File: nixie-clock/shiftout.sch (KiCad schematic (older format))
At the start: 24 parts

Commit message: Added footprints for mini360 buck and nichicon 1uf 250v film cap. Updated nixie-clock schematic with values. Starting to update schematic with daisy-chained configuration now that I figured out the problem with the circuit.
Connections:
- wire segments 171 -> 177
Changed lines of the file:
@@
 Text Notes 5850 3000 0    50   ~ 0
 IN-1\nHours
+Wire Wire Line
+	950  1950 950  2650
+Wire Wire Line
+	950  2650 1400 2650
+Connection ~ 1400 2650
+Wire Wire Line
+	950  5700 950  6400
+Wire Wire Line
+	950  6400 1400 6400
+Connection ~ 1400 6400
+Wire Wire Line
+	5850 4100 5850 4800
+Wire Wire Line
+	5850 4800 6300 4800
+Connection ~ 6300 4800
 $EndSCHEMATC

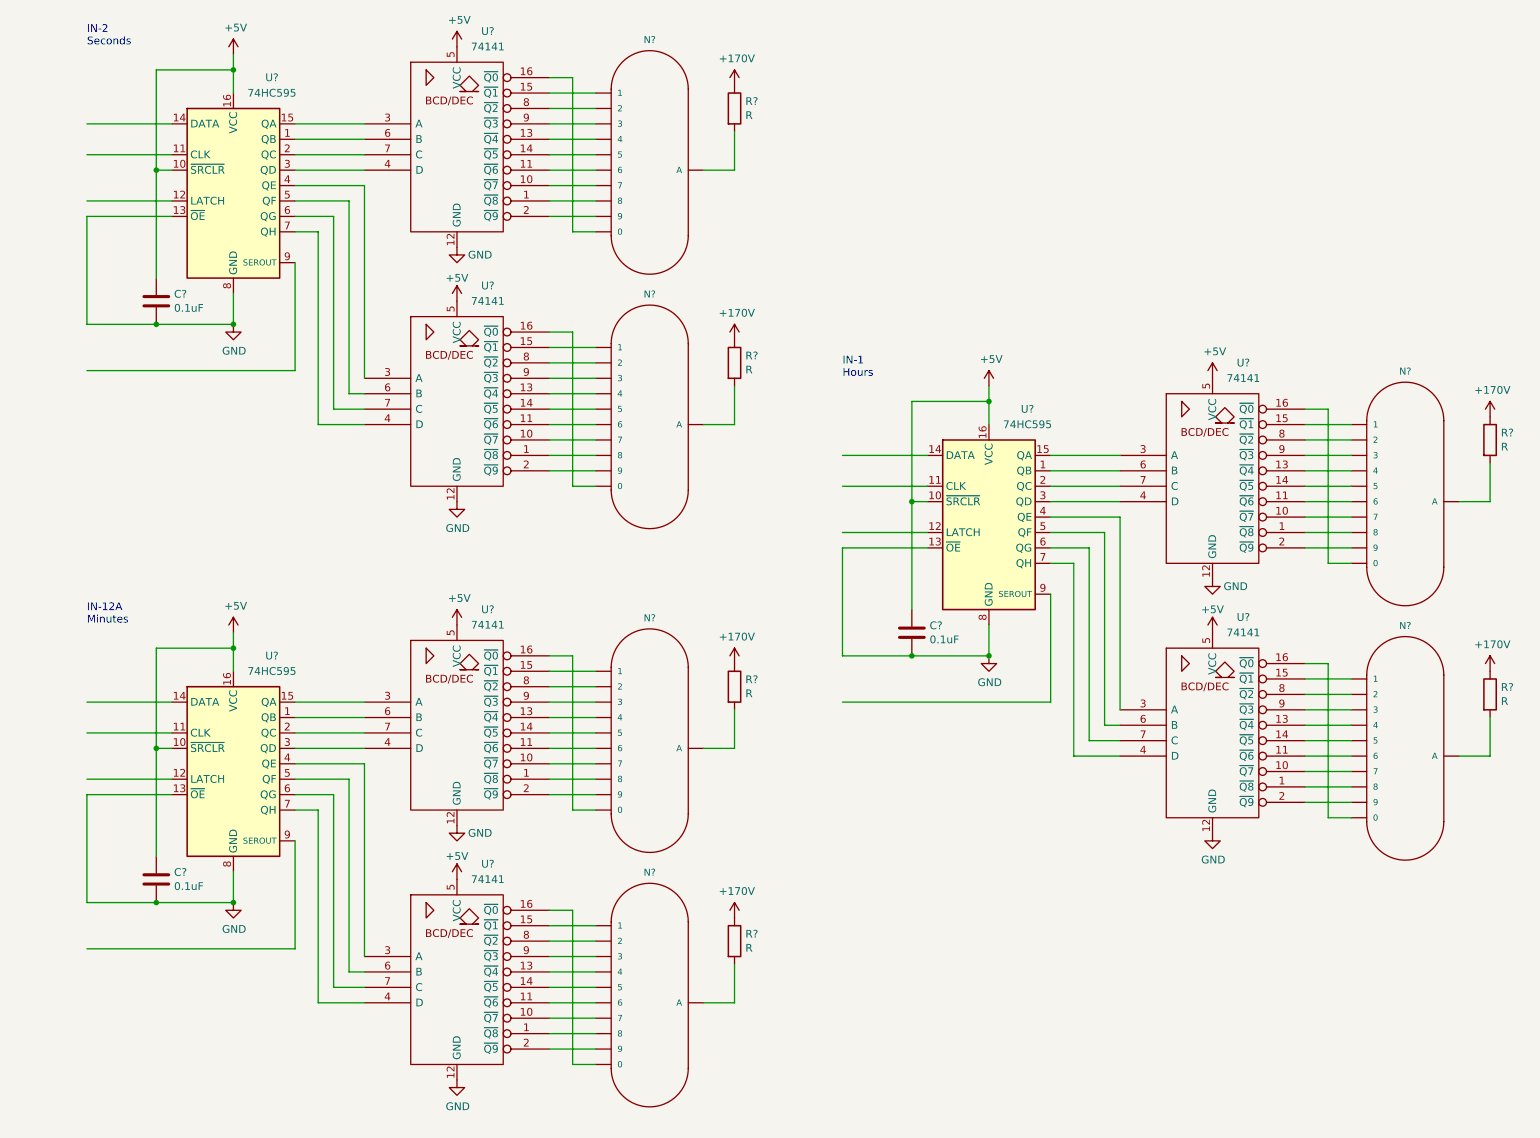
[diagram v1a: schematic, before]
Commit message: Finished schematic for nixie clock main board. Added IN-3 footprint.
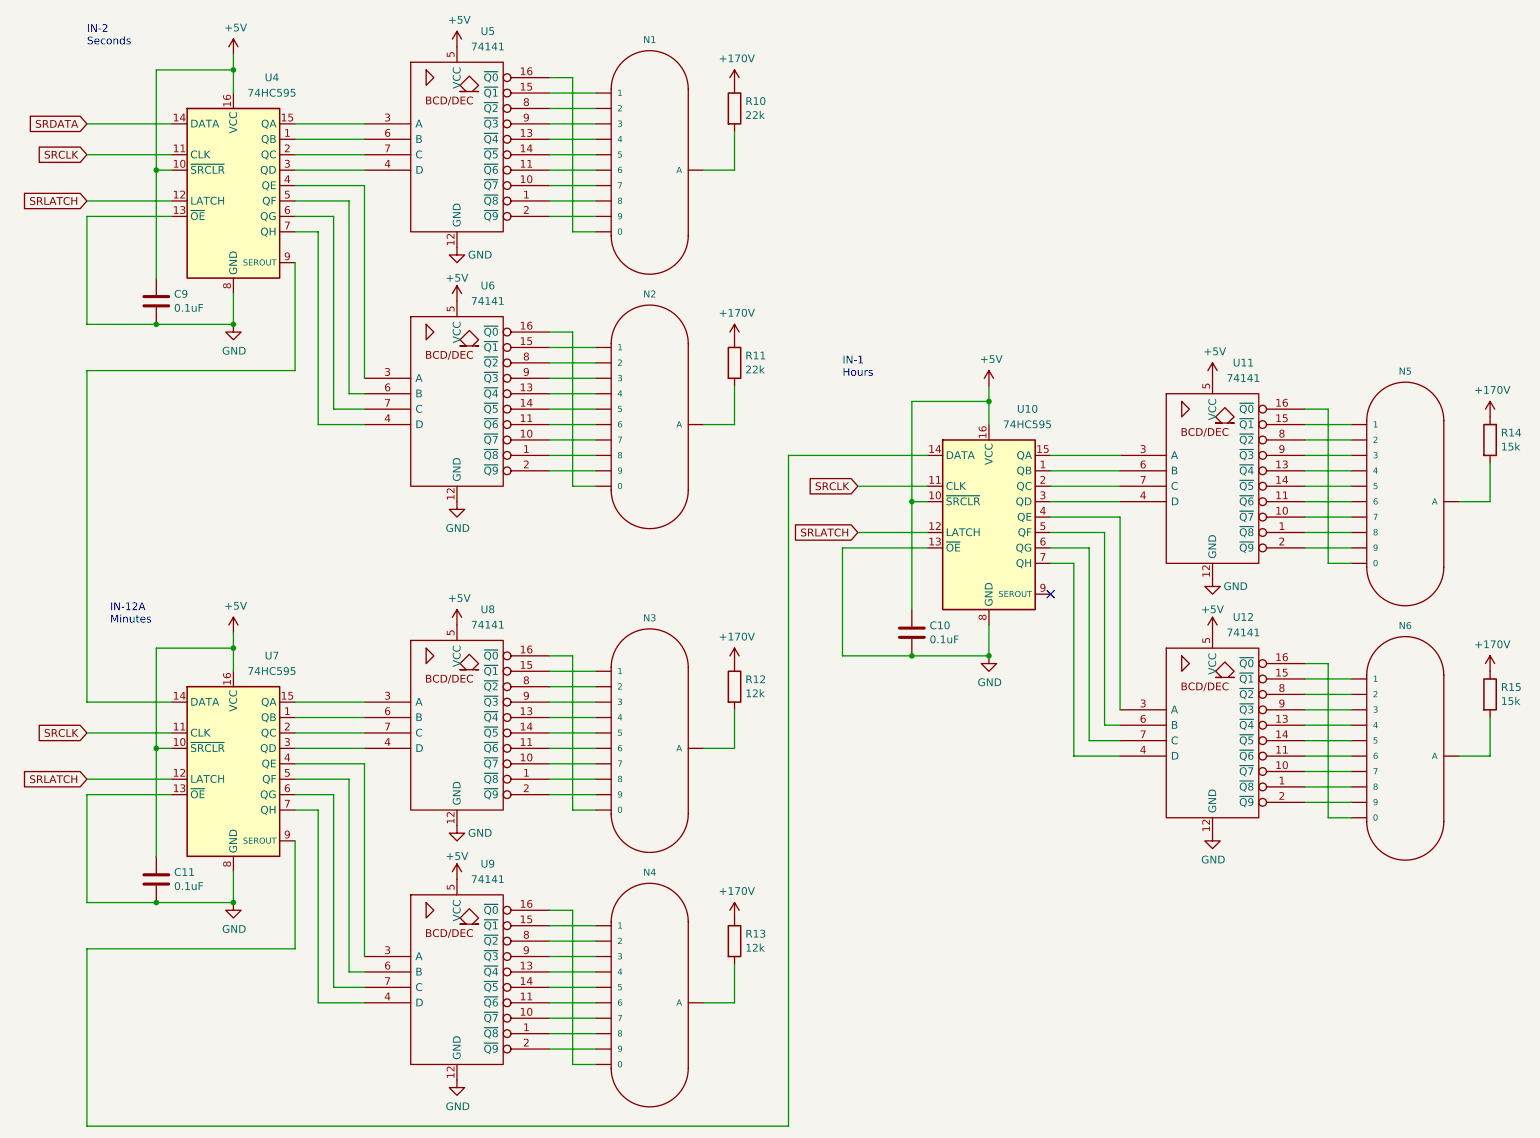
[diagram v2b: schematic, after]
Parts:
- C10, C11, C9: renamed from C?; footprint (none) -> Capacitor_THT:C_Disc_D5.0mm_W2.5mm_P5.00mm
- R10, R11: renamed from R?; value R -> 22k; footprint (none) -> Resistor_THT:R_Axial_DIN0207_L6.3mm_D2.5mm_P10.16mm_Horizontal
- R12, R13: renamed from R?; value R -> 12k; footprint (none) -> Resistor_THT:R_Axial_DIN0207_L6.3mm_D2.5mm_P10.16mm_Horizontal
- R14, R15: renamed from R?; value R -> 15k; footprint (none) -> Resistor_THT:R_Axial_DIN0207_L6.3mm_D2.5mm_P10.16mm_Horizontal
- U10, U11, U12, U4, U5, U6, U7, U8, U9: renamed from U?; footprint (none) -> Package_DIP:DIP-16_W7.62mm_Socket
- gave numbers to parts that had none: 6
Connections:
- net labels added: SRCLK, SRDATA, SRLATCH
- wire segments 177 -> 179
- no-connect marks 0 -> 1

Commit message: Readded pushbuttons to mainboard as an option. Beginning K155ID1-nixie exchange zone.
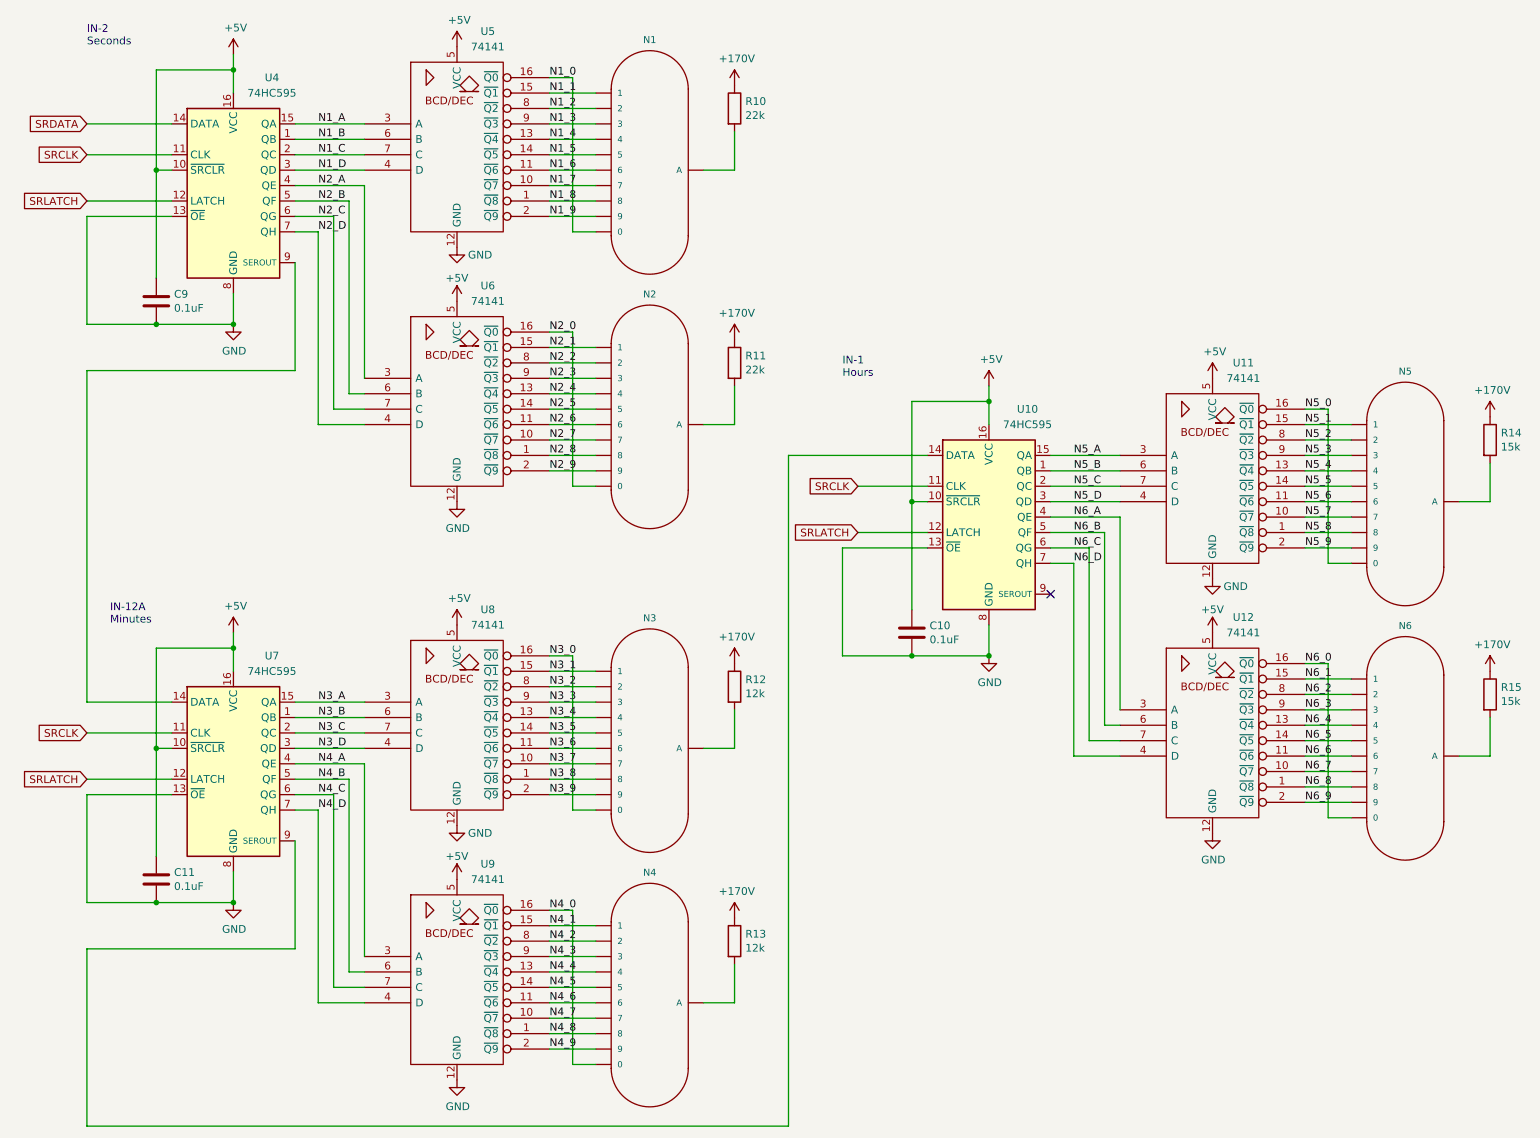
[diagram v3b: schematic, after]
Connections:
- net N2_8: now reaches N2.8, U6.1 (~Q8)
- net N2_7: now reaches N2.7, U6.10 (~Q7)
- net N2_6: now reaches N2.6, U6.11 (~Q6)
- net N2_4: now reaches N2.4, U6.13 (~Q4)
- net N2_5: now reaches N2.5, U6.14 (~Q5)
- net N2_1: now reaches N2.1, U6.15 (~Q1)
- net N2_0: now reaches N2.0, U6.16 (~Q0)
- net N2_9: now reaches N2.9, U6.2 (~Q9)
- net N2_A: now reaches U4.4 (QE), U6.3 (A)
- net N2_D: now reaches U4.7 (QH), U6.4 (D)
- net N2_B: now reaches U4.5 (QF), U6.6 (B)
- net N2_C: now reaches U4.6 (QG), U6.7 (C)
- net N2_2: now reaches N2.2, U6.8 (~Q2)
- net N2_3: now reaches N2.3, U6.9 (~Q3)
- net N1_8: now reaches N1.8, U5.1 (~Q8)
- net N1_7: now reaches N1.7, U5.10 (~Q7)
- net N1_6: now reaches N1.6, U5.11 (~Q6)
- net N1_4: now reaches N1.4, U5.13 (~Q4)
- net N1_5: now reaches N1.5, U5.14 (~Q5)
- net N1_1: now reaches N1.1, U5.15 (~Q1)
- net N1_0: now reaches N1.0, U5.16 (~Q0)
- net N1_9: now reaches N1.9, U5.2 (~Q9)
- net N1_A: now reaches U4.15 (QA), U5.3 (A)
- net N1_D: now reaches U4.3 (QD), U5.4 (D)
- net N1_B: now reaches U4.1 (QB), U5.6 (B)
- net N1_C: now reaches U4.2 (QC), U5.7 (C)
- net N1_2: now reaches N1.2, U5.8 (~Q2)
- net N1_3: now reaches N1.3, U5.9 (~Q3)
- net N4_8: now reaches N4.8, U9.1 (~Q8)
- net N4_7: now reaches N4.7, U9.10 (~Q7)
- net N4_6: now reaches N4.6, U9.11 (~Q6)
- net N4_4: now reaches N4.4, U9.13 (~Q4)
- net N4_5: now reaches N4.5, U9.14 (~Q5)
- net N4_1: now reaches N4.1, U9.15 (~Q1)
- net N4_0: now reaches N4.0, U9.16 (~Q0)
- net N4_9: now reaches N4.9, U9.2 (~Q9)
- net N4_A: now reaches U7.4 (QE), U9.3 (A)
- net N4_D: now reaches U7.7 (QH), U9.4 (D)
- net N4_B: now reaches U7.5 (QF), U9.6 (B)
- net N4_C: now reaches U7.6 (QG), U9.7 (C)
- net N4_2: now reaches N4.2, U9.8 (~Q2)
- net N4_3: now reaches N4.3, U9.9 (~Q3)
- net N3_8: now reaches N3.8, U8.1 (~Q8)
- net N3_7: now reaches N3.7, U8.10 (~Q7)
- net N3_6: now reaches N3.6, U8.11 (~Q6)
- net N3_4: now reaches N3.4, U8.13 (~Q4)
- net N3_5: now reaches N3.5, U8.14 (~Q5)
- net N3_1: now reaches N3.1, U8.15 (~Q1)
- net N3_0: now reaches N3.0, U8.16 (~Q0)
- net N3_9: now reaches N3.9, U8.2 (~Q9)
- net N3_A: now reaches U7.15 (QA), U8.3 (A)
- net N3_D: now reaches U7.3 (QD), U8.4 (D)
- net N3_B: now reaches U7.1 (QB), U8.6 (B)
- net N3_C: now reaches U7.2 (QC), U8.7 (C)
- net N3_2: now reaches N3.2, U8.8 (~Q2)
- net N3_3: now reaches N3.3, U8.9 (~Q3)
- net N6_8: now reaches N6.8, U12.1 (~Q8)
- net N6_7: now reaches N6.7, U12.10 (~Q7)
- net N6_6: now reaches N6.6, U12.11 (~Q6)
- net N6_4: now reaches N6.4, U12.13 (~Q4)
- net N6_5: now reaches N6.5, U12.14 (~Q5)
- net N6_1: now reaches N6.1, U12.15 (~Q1)
- net N6_0: now reaches N6.0, U12.16 (~Q0)
- net N6_9: now reaches N6.9, U12.2 (~Q9)
- net N6_A: now reaches U10.4 (QE), U12.3 (A)
- net N6_D: now reaches U10.7 (QH), U12.4 (D)
- net N6_B: now reaches U10.5 (QF), U12.6 (B)
- net N6_C: now reaches U10.6 (QG), U12.7 (C)
- net N6_2: now reaches N6.2, U12.8 (~Q2)
- net N6_3: now reaches N6.3, U12.9 (~Q3)
- net N5_8: now reaches N5.8, U11.1 (~Q8)
- net N5_7: now reaches N5.7, U11.10 (~Q7)
- net N5_6: now reaches N5.6, U11.11 (~Q6)
- net N5_4: now reaches N5.4, U11.13 (~Q4)
- net N5_5: now reaches N5.5, U11.14 (~Q5)
- net N5_1: now reaches N5.1, U11.15 (~Q1)
- net N5_0: now reaches N5.0, U11.16 (~Q0)
- net N5_9: now reaches N5.9, U11.2 (~Q9)
- net N5_A: now reaches U10.15 (QA), U11.3 (A)
- net N5_D: now reaches U10.3 (QD), U11.4 (D)
- net N5_B: now reaches U10.1 (QB), U11.6 (B)
- net N5_C: now reaches U10.2 (QC), U11.7 (C)
- net N5_2: now reaches N5.2, U11.8 (~Q2)
- net N5_3: now reaches N5.3, U11.9 (~Q3)
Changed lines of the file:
@@
 	1500 1950 950  1950
 Wire Wire Line
-	3950 1150 4250 1150
-Wire Wire Line
 	3950 1250 4250 1250
 Wire Wire Line
@@
 Wire Wire Line
 	4250 2050 4100 2050
-Wire Wire Line
-	4100 2050 4100 1050
 Wire Wire Line
 	4100 1050 3950 1050
@@
 SRLATCH
 NoConn ~ 7200 4400
+Wire Wire Line
+	4100 2050 4100 1050
+Wire Wire Line
+	3950 1150 4250 1150
+Text Label 2450 1350 0    50   ~ 0
+N1_A
+Text Label 2450 1450 0    50   ~ 0
+N1_B
+Text Label 2450 1550 0    50   ~ 0
+N1_C
+Text Label 2450 1650 0    50   ~ 0
+N1_D
+Text Label 2450 1750 0    50   ~ 0
+N2_A
+Text Label 2450 1850 0    50   ~ 0
+N2_B
+Text Label 2450 1950 0    50   ~ 0
+N2_C
+Text Label 2450 2050 0    50   ~ 0
+N2_D
+Text Label 3950 2700 0    50   ~ 0
+N2_0
+Text Label 3950 2800 0    50   ~ 0
+N2_1
+Text Label 3950 2900 0    50   ~ 0
+N2_2
+Text Label 3950 3000 0    50   ~ 0
+N2_3
+Text Label 3950 3100 0    50   ~ 0
+N2_4
+Text Label 3950 3200 0    50   ~ 0
+N2_5
+Text Label 3950 3300 0    50   ~ 0
+N2_6
+Text Label 3950 3400 0    50   ~ 0
+N2_7
+Text Label 3950 3500 0    50   ~ 0
+N2_8
+Text Label 3950 3600 0    50   ~ 0
+N2_9
+Text Label 3950 1050 0    50   ~ 0
+N1_0
+Text Label 3950 1150 0    50   ~ 0
+N1_1
+Text Label 3950 1250 0    50   ~ 0
+N1_2
+Text Label 3950 1350 0    50   ~ 0
+N1_3
+Text Label 3950 1450 0    50   ~ 0
+N1_4
+Text Label 3950 1550 0    50   ~ 0
+N1_5
+Text Label 3950 1650 0    50   ~ 0
+N1_6
+Text Label 3950 1750 0    50   ~ 0
+N1_7
+Text Label 3950 1850 0    50   ~ 0
+N1_8
+Text Label 3950 1950 0    50   ~ 0
+N1_9
+Text Label 2450 5100 0    50   ~ 0
+N3_A
+Text Label 2450 5200 0    50   ~ 0
+N3_B
+Text Label 2450 5300 0    50   ~ 0
+N3_C
+Text Label 2450 5400 0    50   ~ 0
+N3_D
+Text Label 2450 5500 0    50   ~ 0
+N4_A
+Text Label 2450 5600 0    50   ~ 0
+N4_B
+Text Label 2450 5700 0    50   ~ 0
+N4_C
+Text Label 2450 5800 0    50   ~ 0
+N4_D
+Text Label 3950 4800 0    50   ~ 0
+N3_0
+Text Label 3950 4900 0    50   ~ 0
+N3_1
+Text Label 3950 5000 0    50   ~ 0
+N3_2
+Text Label 3950 5100 0    50   ~ 0
+N3_3
+Text Label 3950 5200 0    50   ~ 0
+N3_4
+Text Label 3950 5300 0    50   ~ 0
+N3_5
+Text Label 3950 5400 0    50   ~ 0
+N3_6
+Text Label 3950 5500 0    50   ~ 0
+N3_7
+Text Label 3950 5600 0    50   ~ 0
+N3_8
+Text Label 3950 5700 0    50   ~ 0
+N3_9
+Text Label 3950 6450 0    50   ~ 0
+N4_0
+Text Label 3950 6550 0    50   ~ 0
+N4_1
+Text Label 3950 6650 0    50   ~ 0
+N4_2
+Text Label 3950 6750 0    50   ~ 0
+N4_3
+Text Label 3950 6850 0    50   ~ 0
+N4_4
+Text Label 3950 6950 0    50   ~ 0
+N4_5
+Text Label 3950 7050 0    50   ~ 0
+N4_6
+Text Label 3950 7150 0    50   ~ 0
+N4_7
+Text Label 3950 7250 0    50   ~ 0
+N4_8
+Text Label 3950 7350 0    50   ~ 0
+N4_9
+Text Label 8850 3200 0    50   ~ 0
+N5_0
+Text Label 8850 3300 0    50   ~ 0
+N5_1
+Text Label 8850 3400 0    50   ~ 0
+N5_2
+Text Label 8850 3500 0    50   ~ 0
+N5_3
+Text Label 8850 3600 0    50   ~ 0
+N5_4
+Text Label 8850 3700 0    50   ~ 0
+N5_5
+Text Label 8850 3800 0    50   ~ 0
+N5_6
+Text Label 8850 3900 0    50   ~ 0
+N5_7
+Text Label 8850 4000 0    50   ~ 0
+N5_8
+Text Label 8850 4100 0    50   ~ 0
+N5_9
+Text Label 7350 3500 0    50   ~ 0
+N5_A
+Text Label 7350 3600 0    50   ~ 0
+N5_B
+Text Label 7350 3700 0    50   ~ 0
+N5_C
+Text Label 7350 3800 0    50   ~ 0
+N5_D
+Text Label 7350 3900 0    50   ~ 0
+N6_A
+Text Label 7350 4000 0    50   ~ 0
+N6_B
+Text Label 7350 4100 0    50   ~ 0
+N6_C
+Text Label 7350 4200 0    50   ~ 0
+N6_D
+Text Label 8850 4850 0    50   ~ 0
+N6_0
+Text Label 8850 4950 0    50   ~ 0
+N6_1
+Text Label 8850 5050 0    50   ~ 0
+N6_2
+Text Label 8850 5150 0    50   ~ 0
+N6_3
+Text Label 8850 5250 0    50   ~ 0
+N6_4
+Text Label 8850 5350 0    50   ~ 0
+N6_5
+Text Label 8850 5450 0    50   ~ 0
+N6_6
+Text Label 8850 5550 0    50   ~ 0
+N6_7
+Text Label 8850 5650 0    50   ~ 0
+N6_8
+Text Label 8850 5750 0    50   ~ 0
+N6_9
 $EndSCHEMATC
